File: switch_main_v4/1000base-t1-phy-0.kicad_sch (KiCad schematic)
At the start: 39 parts, among them Q1301 DMN21D2UFB-7B, Q1302 DMP21D0UFB-7B, U1301 TPS62290TDRVRQ1, U1302 88Q2112-A2-NYD2A000-P123

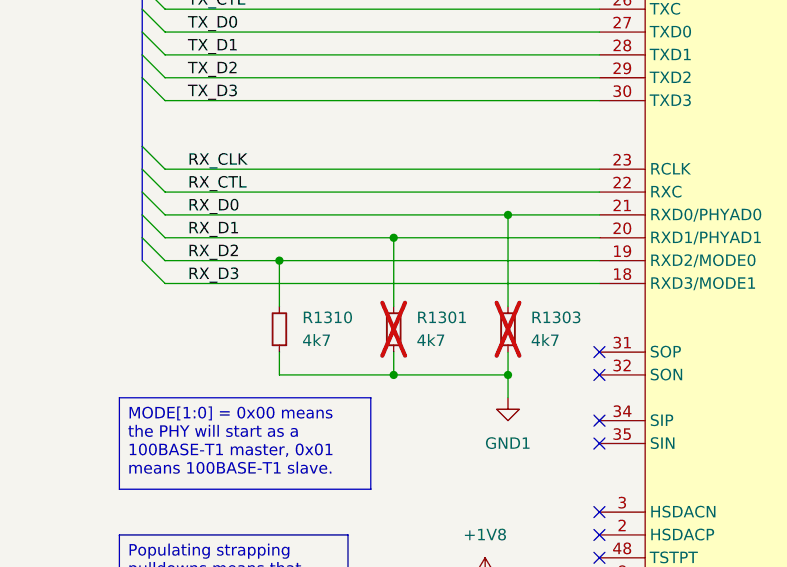
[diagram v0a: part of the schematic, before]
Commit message: Fixed mistake where RMII TX and RX signals were swapped
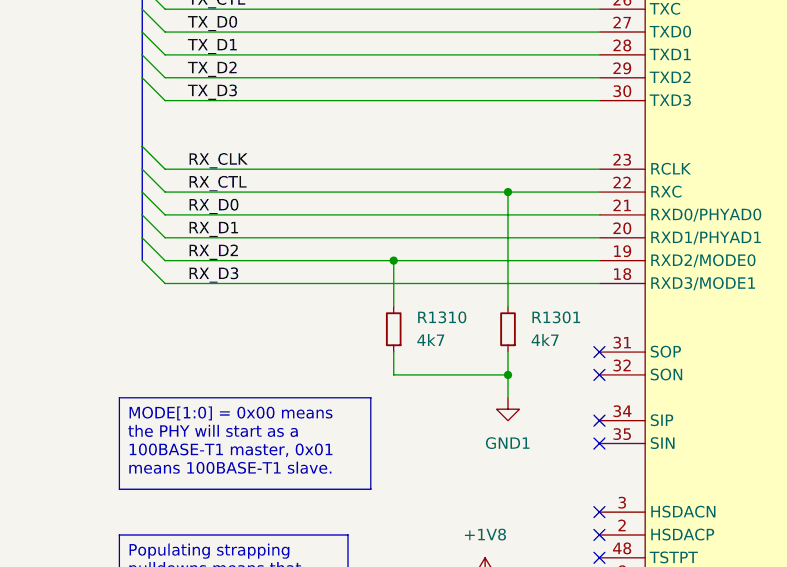
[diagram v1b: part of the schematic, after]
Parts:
- removed R1303: 4k7, Resistor_SMD:R_0402_1005Metric, symbol Device:R_Small
- R1301: now fitted; now in the parts list
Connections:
- net RX_CTL: now also R1301.2
- net RX_D1: no longer R1301.2
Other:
- moved on the sheet: R1310
